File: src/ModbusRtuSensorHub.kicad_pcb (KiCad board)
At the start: 2 copper layers, 30.5 x 31.8 mm, 17 parts, among them U2 ATtiny3216-S

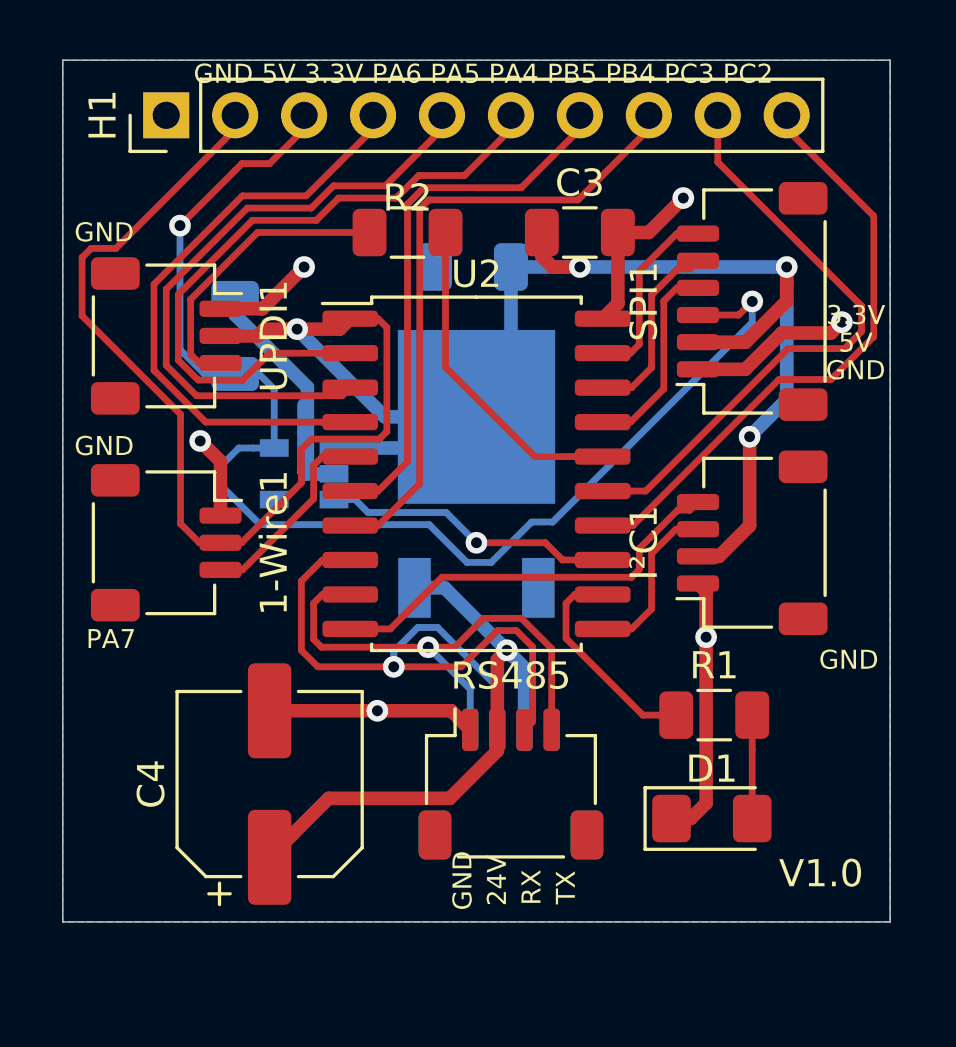
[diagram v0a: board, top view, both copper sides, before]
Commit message: updated pcb with onboard transciever
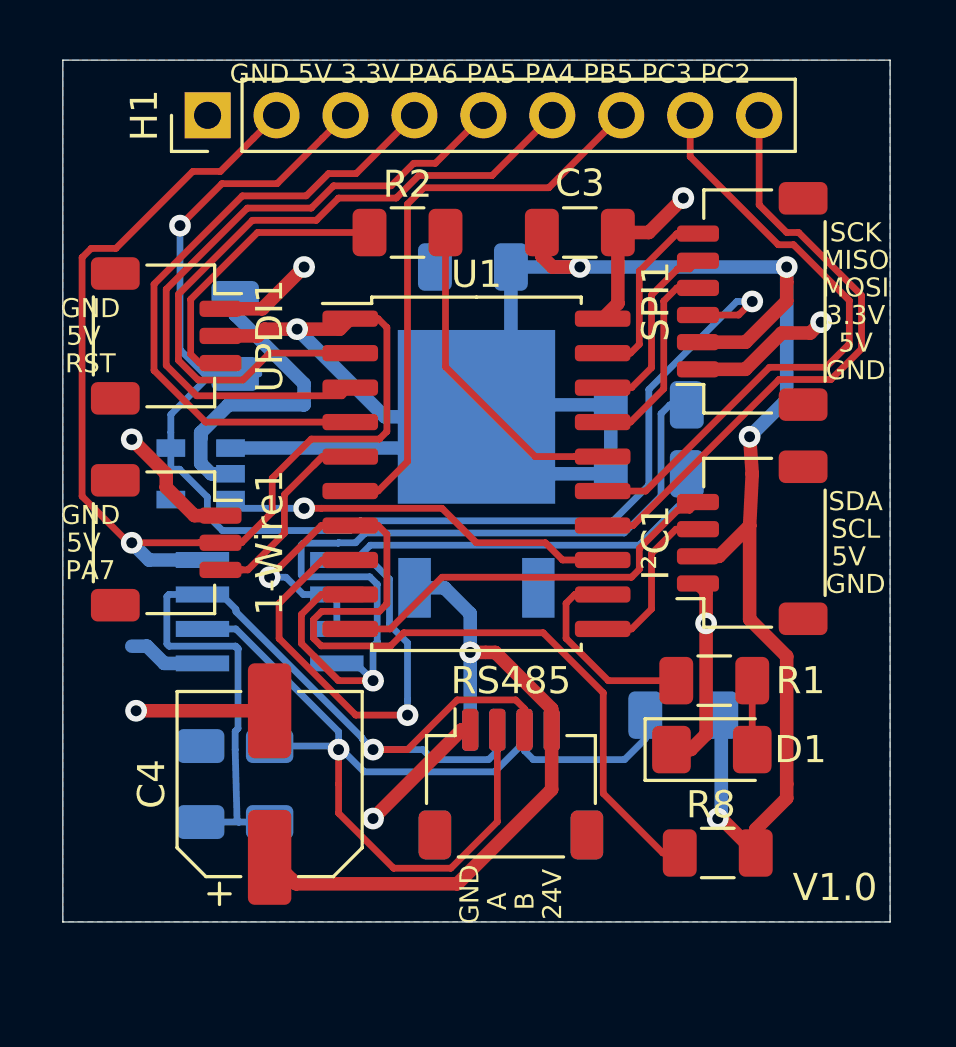
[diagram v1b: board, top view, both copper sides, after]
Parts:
- added R3: 120, Resistor_SMD:R_1206_3216Metric, B.Cu at (190.5, 110.5)
- added R4: 10k, Resistor_SMD:R_1206_3216Metric, B.Cu at (205.7, 108.0)
- added R5: 10k, Resistor_SMD:R_1206_3216Metric, B.Cu at (188.0, 110.5)
- added R6: 10k, Resistor_SMD:R_1206_3216Metric, B.Cu at (204.5, 99.1)
- added R7: 10k, Resistor_SMD:R_1206_3216Metric, B.Cu at (204.5, 96.5)
- added R8: 10k, Resistor_SMD:R_1206_3216Metric, F.Cu at (207.0, 113.0)
- added U2: MAX1487CSA+T, MAX1487CSA_T:SOIC127P600X175-8N, B.Cu at (190.5, 104.1)
- H1: value Conn_01x10 -> Conn_01x9; footprint Connector_PinHeader_2.54mm:PinHeader_1x10_P2.54mm_Vertical -> Connector_PinHeader_2.54mm:PinHeader_1x09_P2.54mm_Vertical
- moved LDO2 3.81 mm to (188.0, 99.1)
- moved D1 2.54 mm to (206.8, 109.2)
- moved H1 1.52 mm to (188.2, 85.9)
- moved R1 1.27 mm to (206.9, 106.7)
- renumbered RS485_2 to RS485, U2 to U1
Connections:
- H1 pad 8: /PB4 -> /PC3
- H1 pad 9: /PC3 -> /PC2
- RS485 pad 2: /24V -> /A (x2)
- RS485 pad 3: /RX -> /B (x2)
- RS485 pad 4: /TX -> /24V (x2)
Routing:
- net /5V: track 88.9 -> 132.0 mm, vias 4 -> 6
- net /A: track 0.00 -> 38.3 mm, vias 0 -> 1
- net /B: track 0.00 -> 36.7 mm, vias 0 -> 1
- net /TX: track 19.3 -> 35.1 mm
- net /PB4: track 23.0 -> 35.5 mm, vias 0 -> 1
- net /RX: track 24.7 -> 32.7 mm
- net /24V: track 21.6 -> 25.9 mm
- net /3.3V: track 47.2 -> 51.2 mm
- net Net-(LDO2-Pad3): track 10.8 -> 14.6 mm
- net /GND: track 48.6 -> 51.9 mm, vias 6 -> 7
- net /PA5: track 22.8 -> 24.5 mm
- net /PA4: track 24.2 -> 26.0 mm
- net /PA6: track 21.6 -> 23.4 mm
- net /PB5: track 19.5 -> 21.3 mm
- net /PA7: track 7.23 -> 8.61 mm
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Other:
- board text added: "A"
- board text added: "B"
- board text added: "GND 5V 3.3V PA6 PA5 PA4 PB5 PC3 PC2"
- board text added: "MISO"
- board text added: "MOSI"
- board text added: "RST"
- board text added: "SCK"
- board text added: "SCL"
- board text added: "SDA"
- board text removed: "GND 5V 3.3V PA6 PA5 PA4 PB5 PB4 PC3 PC2"
- board text removed: "RX"
- board text removed: "TX"

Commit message: latest version
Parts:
- removed the RS485 at (199.4, 110.5)
- RS485: footprint Connector_JST:JST_SH_SM04B-SRSS-TB_1x04-1MP_P1.00mm_Horizontal -> Connector_JST:JST_XH_S4B-XH-A-1_1x04_P2.50mm_Horizontal
- moved R4 7.77 mm to (198.1, 106.4)
- moved RS485 4.58 mm to (194.8, 110.2)
- moved C4 2.81 mm to (187.7, 110.7)
- moved R8 2.05 mm to (208.0, 114.8)
- moved D1 2.02 mm to (208.5, 110.2)
- moved R1 1.73 mm to (208.5, 107.2)
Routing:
- net /5V: track 132.0 -> 173.8 mm
- net /A: track 38.3 -> 17.3 mm, vias 1 -> 0
- net /B: track 36.7 -> 29.7 mm, vias 1 -> 0
- net /GND: track 51.9 -> 46.3 mm, vias 7 -> 6
- net /24V: track 25.9 -> 28.6 mm, vias 1 -> 0
- net Net-(R1-Pad1): track 7.48 -> 9.35 mm
- net /PB4: track 35.5 -> 33.8 mm
- net /RX: track 32.7 -> 31.5 mm
- net /TX: track 35.1 -> 36.0 mm
- net /3.3V: track 51.2 -> 50.3 mm
- net Net-(D1-Pad2): track 2.54 -> 3.08 mm
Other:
- board size 30.5 x 31.8 mm -> 30.7 x 34.3 mm
- rule via_min_size: 0.4 -> 0.5
- board text added: "V1.1"
- board text removed: "V1.0"
